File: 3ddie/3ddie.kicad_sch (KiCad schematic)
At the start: 40 parts

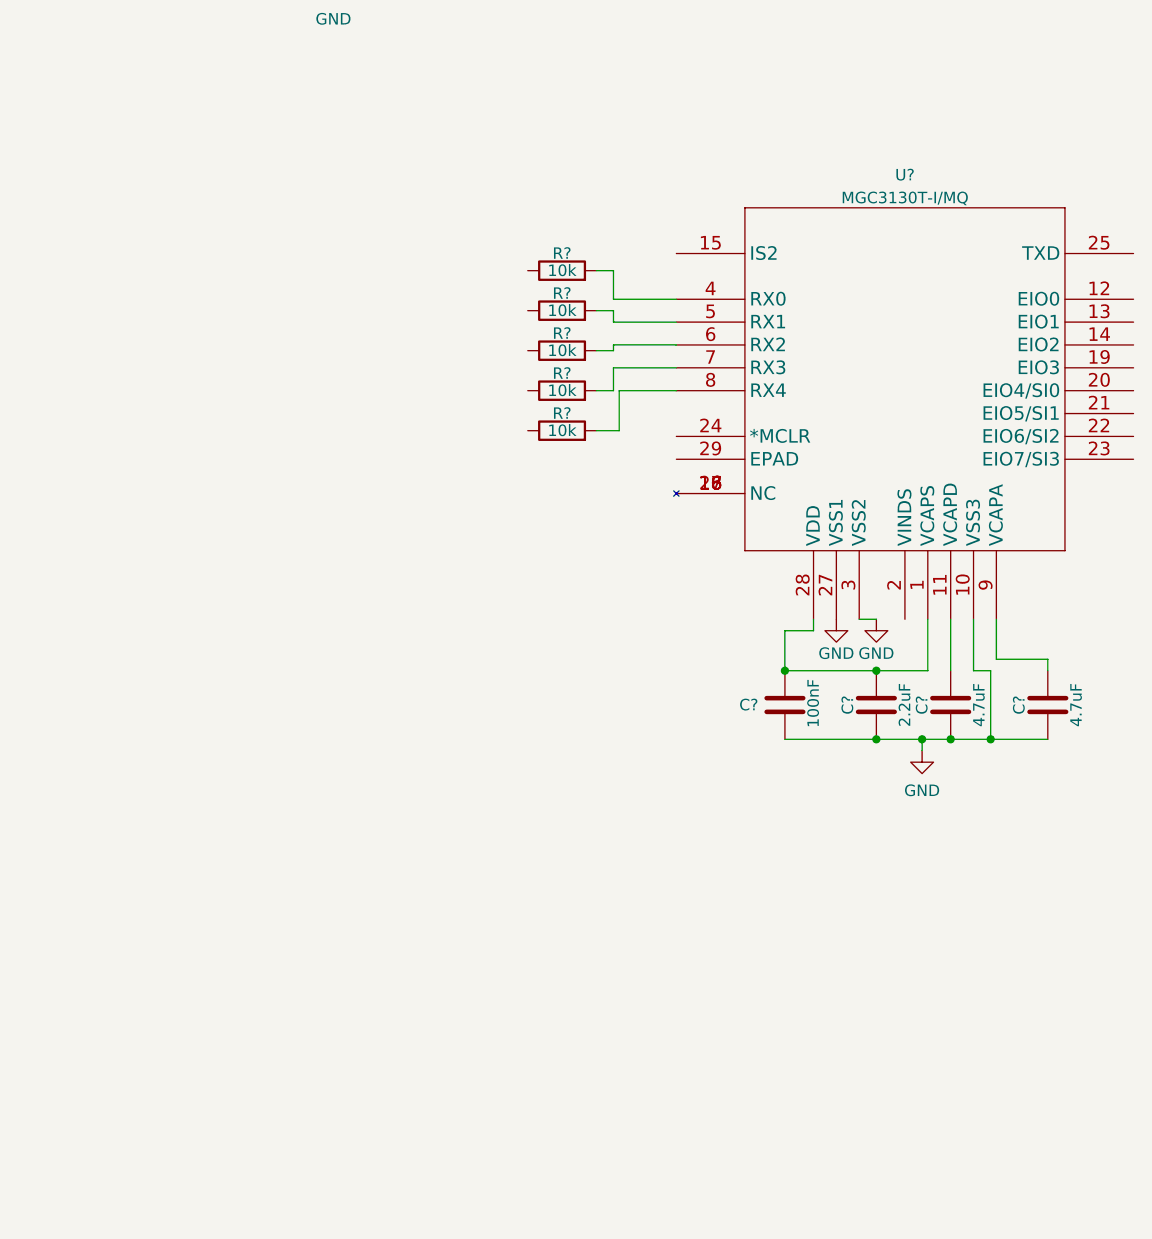
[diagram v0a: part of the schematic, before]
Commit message: fix MGC3130 symbol and footprint, update schema
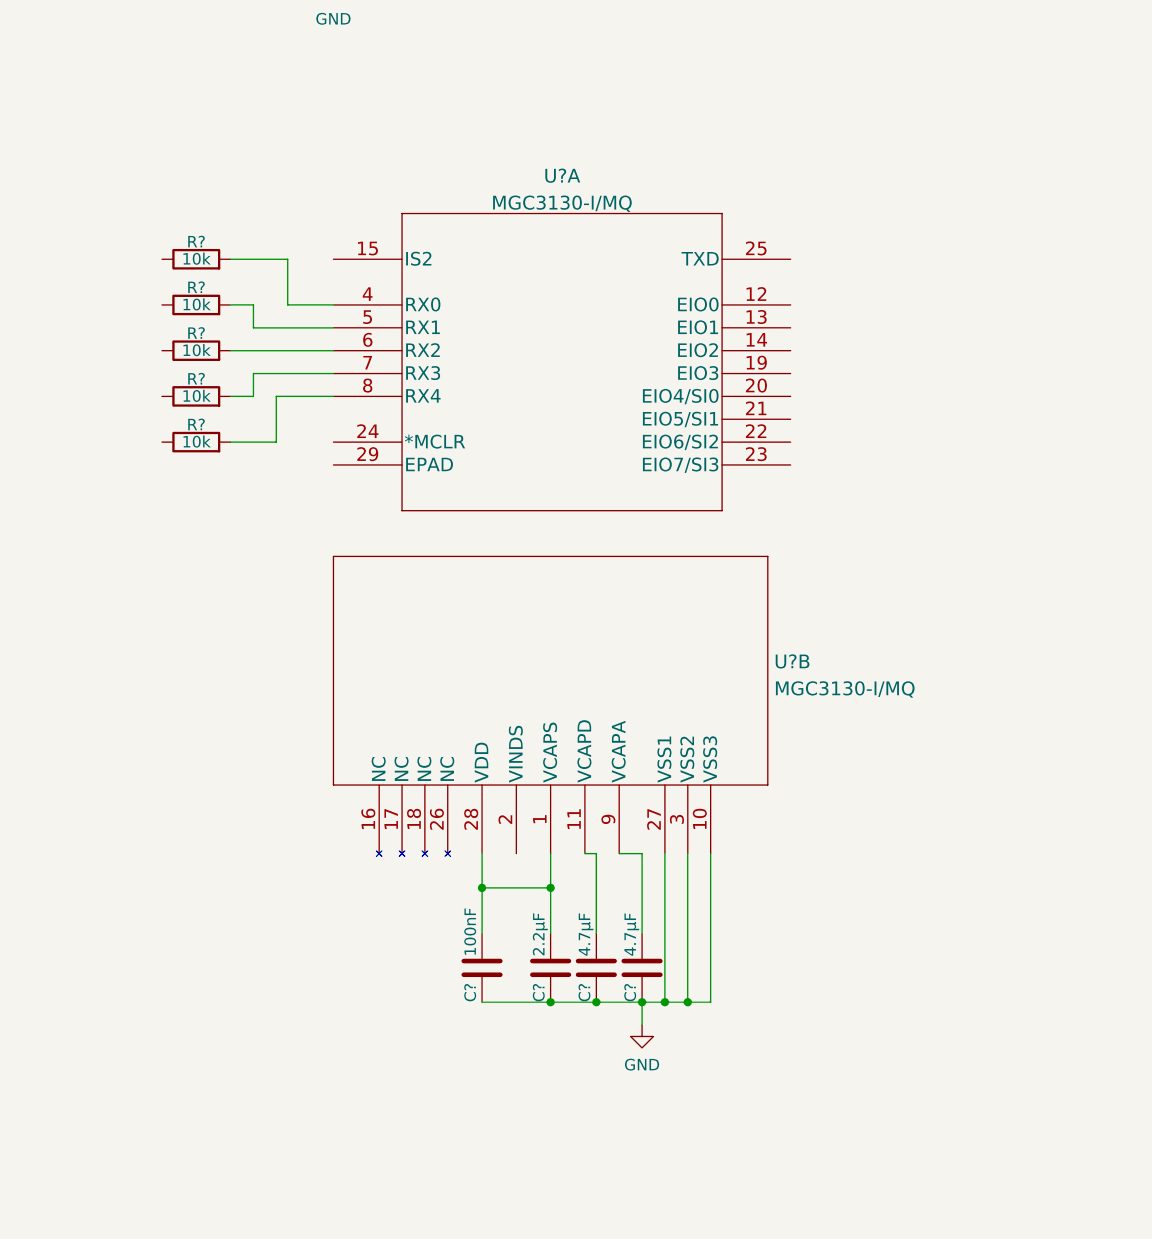
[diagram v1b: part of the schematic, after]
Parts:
- removed C?: 100nF, symbol Device:C
- removed C?: 2.2uF, symbol Device:C
- removed C? (x2): 4.7uF, symbol Device:C
- removed U?: MGC3130T-I/MQ, symbol 3ddie:MGC3130T-I/MQ
- added C? (x2): 4.7μF, symbol Device:C
- added C?: 2.2μF, symbol Device:C
- added C?: 100nF, symbol Device:C
- added U?: MGC3130-I/MQ, QFN28_5X5MQ_MCH, symbol 3ddie:MGC3130-I{brace}slash}MQ
- added U?: MGC3130-I/MQ, QFN28_5X5MQ_MCH, symbol 3ddie:MGC3130-I{brace}slash}MQ
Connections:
- net GND: now also C?.1, C?.1, C?.1, C?.1, U?.10 (VSS3), U?.27 (VSS1), U?.3 (VSS2)
- net at R?.2: now also U?.4 (RX0)
- net at R?.2: now also U?.5 (RX1)
- net at R?.2: now also U?.6 (RX2)
- net at R?.2: now also U?.7 (RX3)
- net at R?.2: now also U?.8 (RX4)
- new net: C?.2, U?.9 (VCAPA)
- new net: C?.2, C?.2, U?.1 (VCAPS), U?.28 (VDD)
- new net: C?.2, U?.11 (VCAPD)
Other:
- moved on the sheet: R?

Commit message: In-class work 10/25
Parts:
- added R? (x2): 1.8k, symbol Device:R
- added R?: 10k, symbol Device:R
- added U?: MCP1416R, Package_TO_SOT_SMD:SOT-23-5, symbol Driver_FET:MCP1416R
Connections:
- net +3V3: now also R?.1, R?.1, R?.2
- net GND: now also U?.13 (EIO1), U?.15 (IS2), U?.29 (EPAD), U?.2 (GND)
- net GPIO12: now also U?.20 (EIO4/SI0), R?.2
- net GPIO13: now also U?.21 (EIO5/SI1), R?.2
- net GPIO14: now also U?.12 (EIO0), R?.1
- net RUN: now also U?.24 (*MCLR)
- net VBUS: now also U?.5 (Vdd)
- net at U?.25 (TXD): now also U?.3 (IN)
- new net 5V_TX: U?.4 (OUT)
- no-connect marks 2 -> 6
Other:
- moved on the sheet: D?, R?

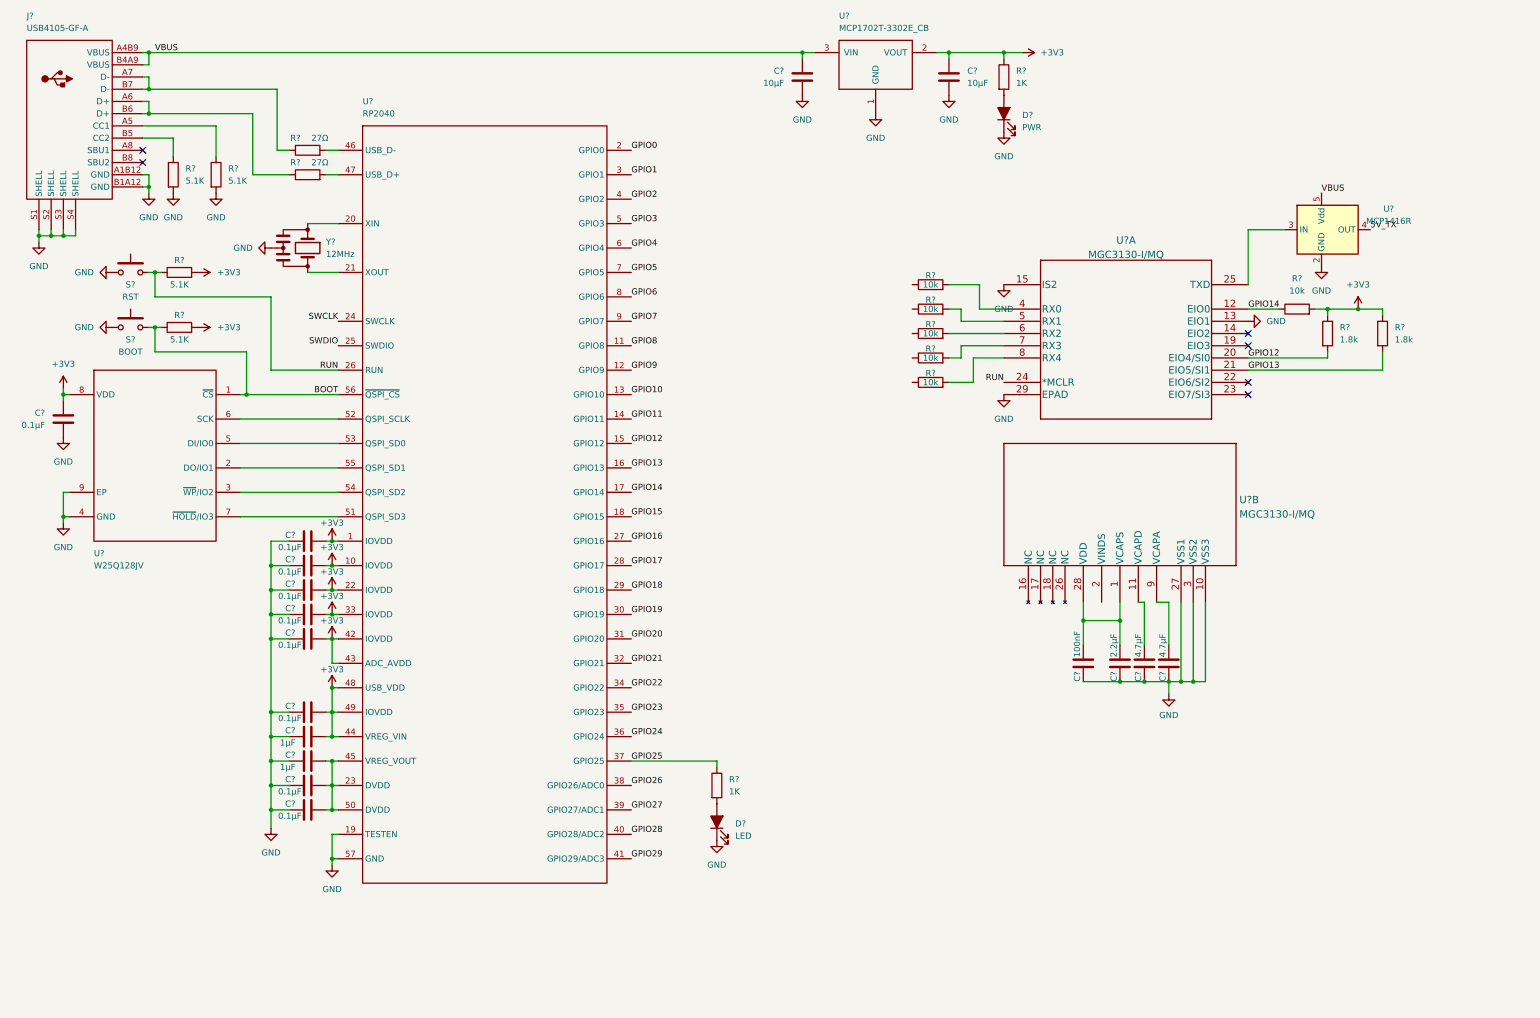
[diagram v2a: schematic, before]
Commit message: connect electrodes, fill in title block, annotate symbols
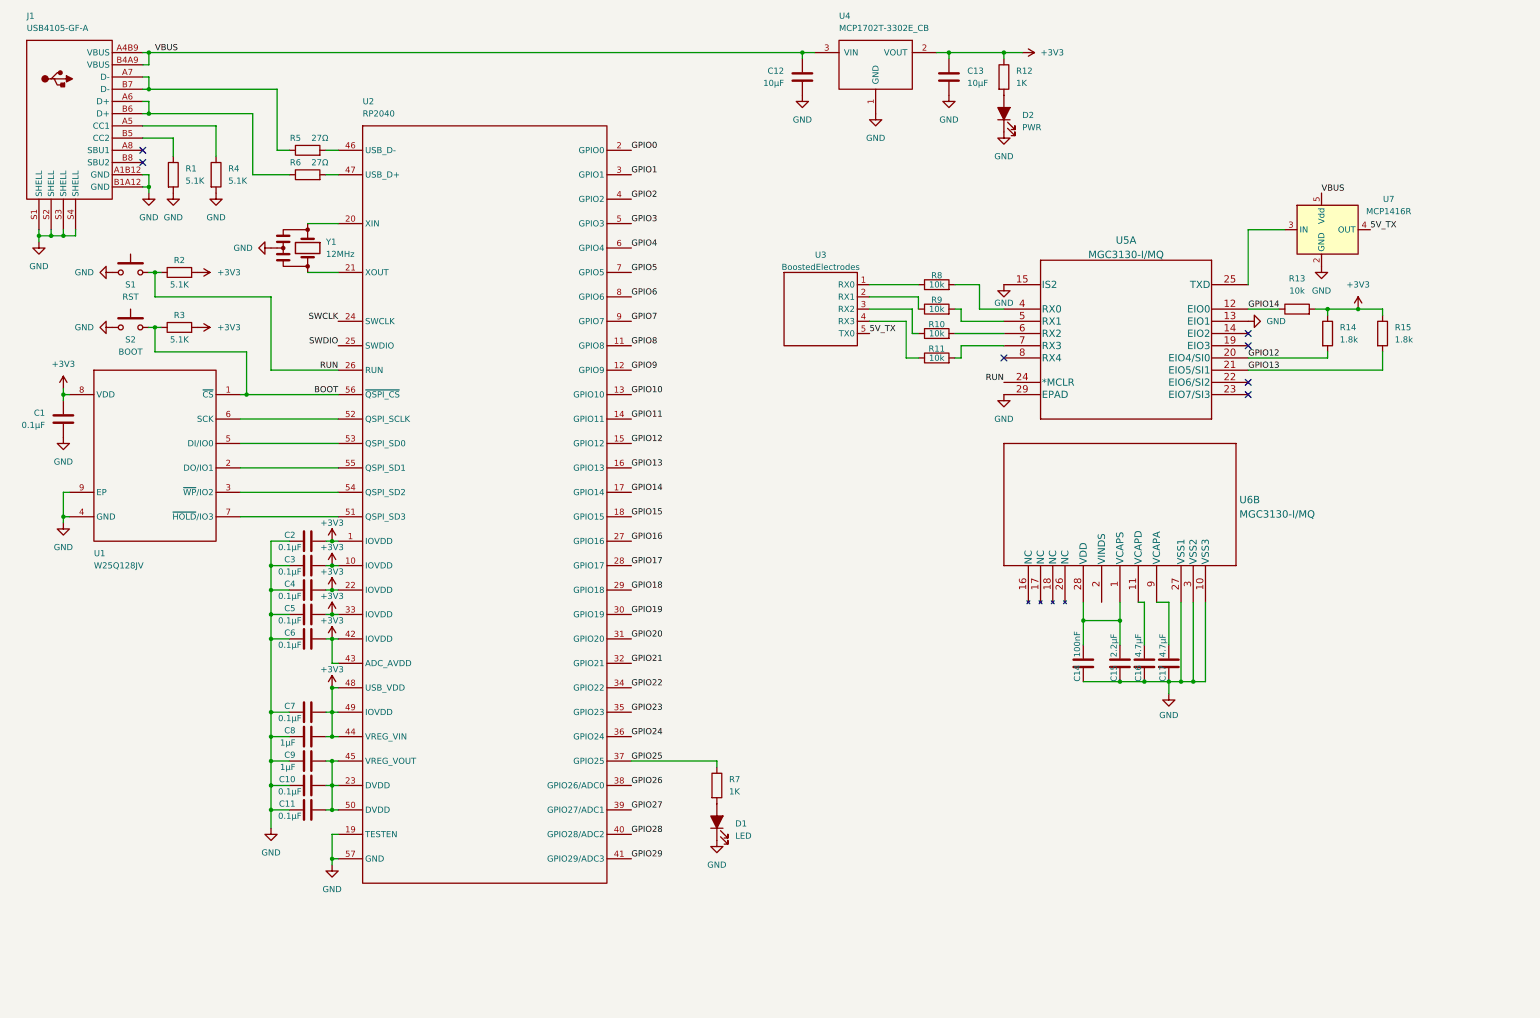
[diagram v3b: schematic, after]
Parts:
- removed R?: 10k, symbol Device:R
- added U3: BoostedElectrodes, symbol 3ddie:BoostedElectrodes
- gave numbers to parts that had none: 44
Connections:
- net 5V_TX: now also U3.5 (TX0)
- net at R10.1: now also U3.3 (RX2)
- net at R11.1: now also U3.4 (RX3)
- net at R8.1: now also U3.1 (RX0)
- net at R9.1: now also U3.2 (RX1)
- no-connect marks 6 -> 7
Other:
- company: (none) -> Jacob Smilg, Grant Miner, & Max Stopyra
- title: (none) -> 3ddie
- moved on the sheet: R10, R11, R8, R9

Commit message: adding midi connectors and dac
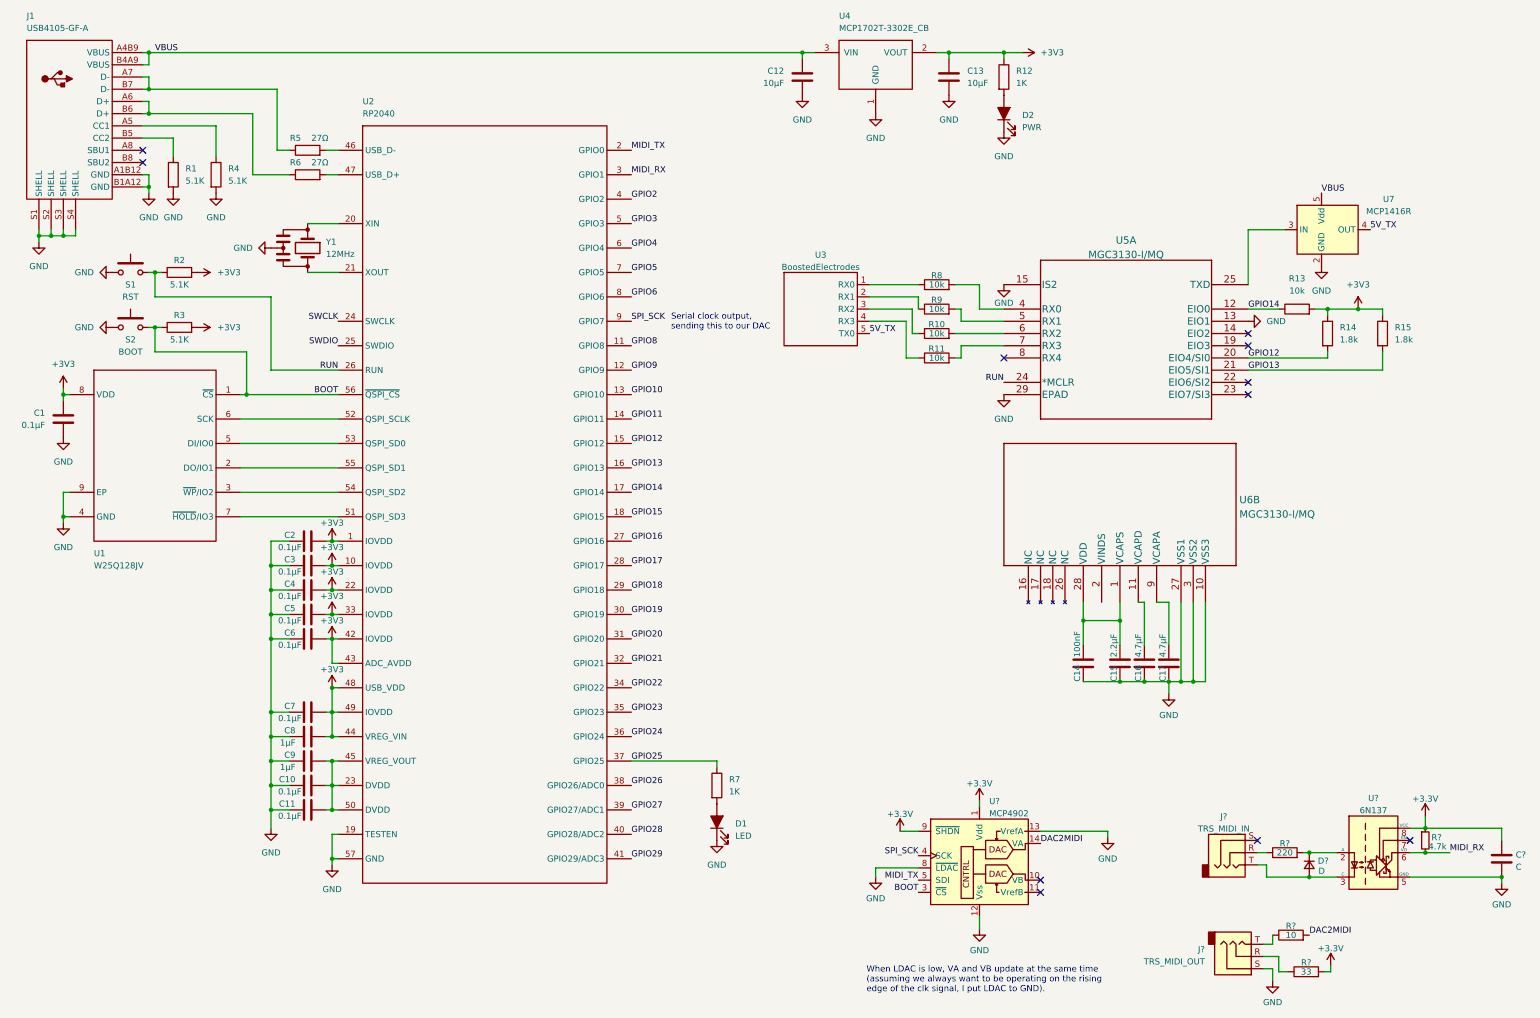
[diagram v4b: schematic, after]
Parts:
- added C?: C, symbol Device:C
- added D?: D, symbol Device:D_Small
- added J?: TRS_MIDI_OUT, symbol Connector:AudioJack3
- added J?: TRS_MIDI_IN, symbol Connector:AudioJack3
- added R?: 10, symbol Device:R
- added R?: 33, symbol Device:R
- added R?: 4.7k, symbol Device:R_Small
- added R?: 220, symbol Device:R
- added U?: MCP4902, symbol Analog_DAC:MCP4902
- added U?: 6N137, Package_DIP:DIP-8_W7.62mm, symbol Isolator:6N137
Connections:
- net BOOT: now also U?.3 (~{CS})
- net GND: now also C?.2, J?.S, U?.12 (Vss), U?.13 (VrefA), U?.5 (GND), U?.8 (~{LDAC})
- net GPIO0 renamed MIDI_TX
- net MIDI_TX: now also U?.5 (SDI)
- net GPIO1 renamed MIDI_RX
- net MIDI_RX: now also R?.2, U?.6 (VO)
- net GPIO7 renamed SPI_SCK
- net SPI_SCK: now also U?.4 (SCK)
- new net: J?.T, R?.1
- new net: J?.R, R?.1 (x2)
- new net: D?.2 (A), J?.T, U?.3 (C)
- new net: D?.1 (K), R?.2, U?.2 (A)
- new net +3.3V: C?.1, R?.1, R?.2, U?.1 (Vdd), U?.8 (VCC), U?.9 (~{SHDN})
- new net DAC2MIDI: R?.2, U?.14 (VA)
- no-connect marks 7 -> 11
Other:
- note added: "Serial clock output, sending this to our DAC"
- note added: "When LDAC is low, VA and VB update at the same time (assuming we always want to be operating on the rising edge of the clk signal, I put LDAC to GND)."

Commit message: Remove DAC, rename pins from schem review
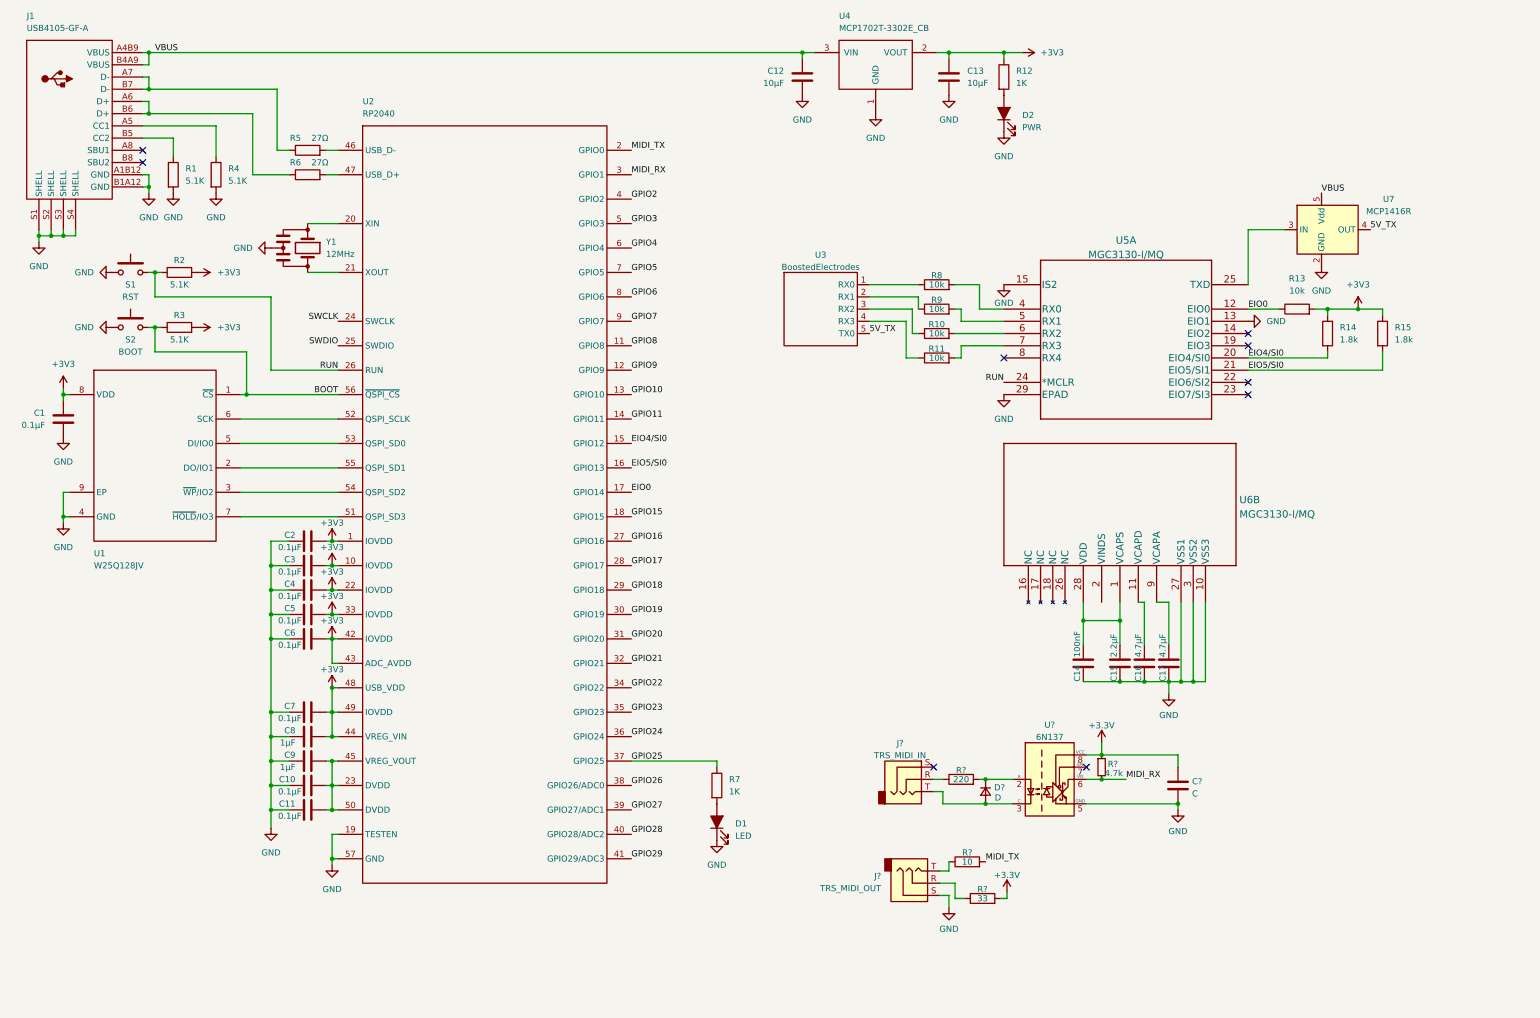
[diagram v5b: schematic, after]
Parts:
- removed U?: MCP4902, symbol Analog_DAC:MCP4902
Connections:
- net DAC2MIDI is gone; now on net MIDI_TX: R?.2
- net GPIO12 renamed EIO4/SI0
- net GPIO13 renamed EIO5/SI0
- net GPIO14 renamed EIO0
- net SPI_SCK renamed GPIO7
- no-connect marks 11 -> 9
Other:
- note removed: "Serial clock output, sending this to our DAC"
- note removed: "When LDAC is low, VA and VB update at the same time (assuming we always want to be operating on the rising edge of the clk signal, I put LDAC to GND)."
- moved on the sheet: C?, D?, J?, R?, U?
